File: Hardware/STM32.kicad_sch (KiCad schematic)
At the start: 73 parts, among them IC1 STTS22HTR, U3 STM32L4R5ZITx, Y2 ECS-TXO-2520-33-250-AN-TR, Y3 TG-3541CE_32.7680KXB3

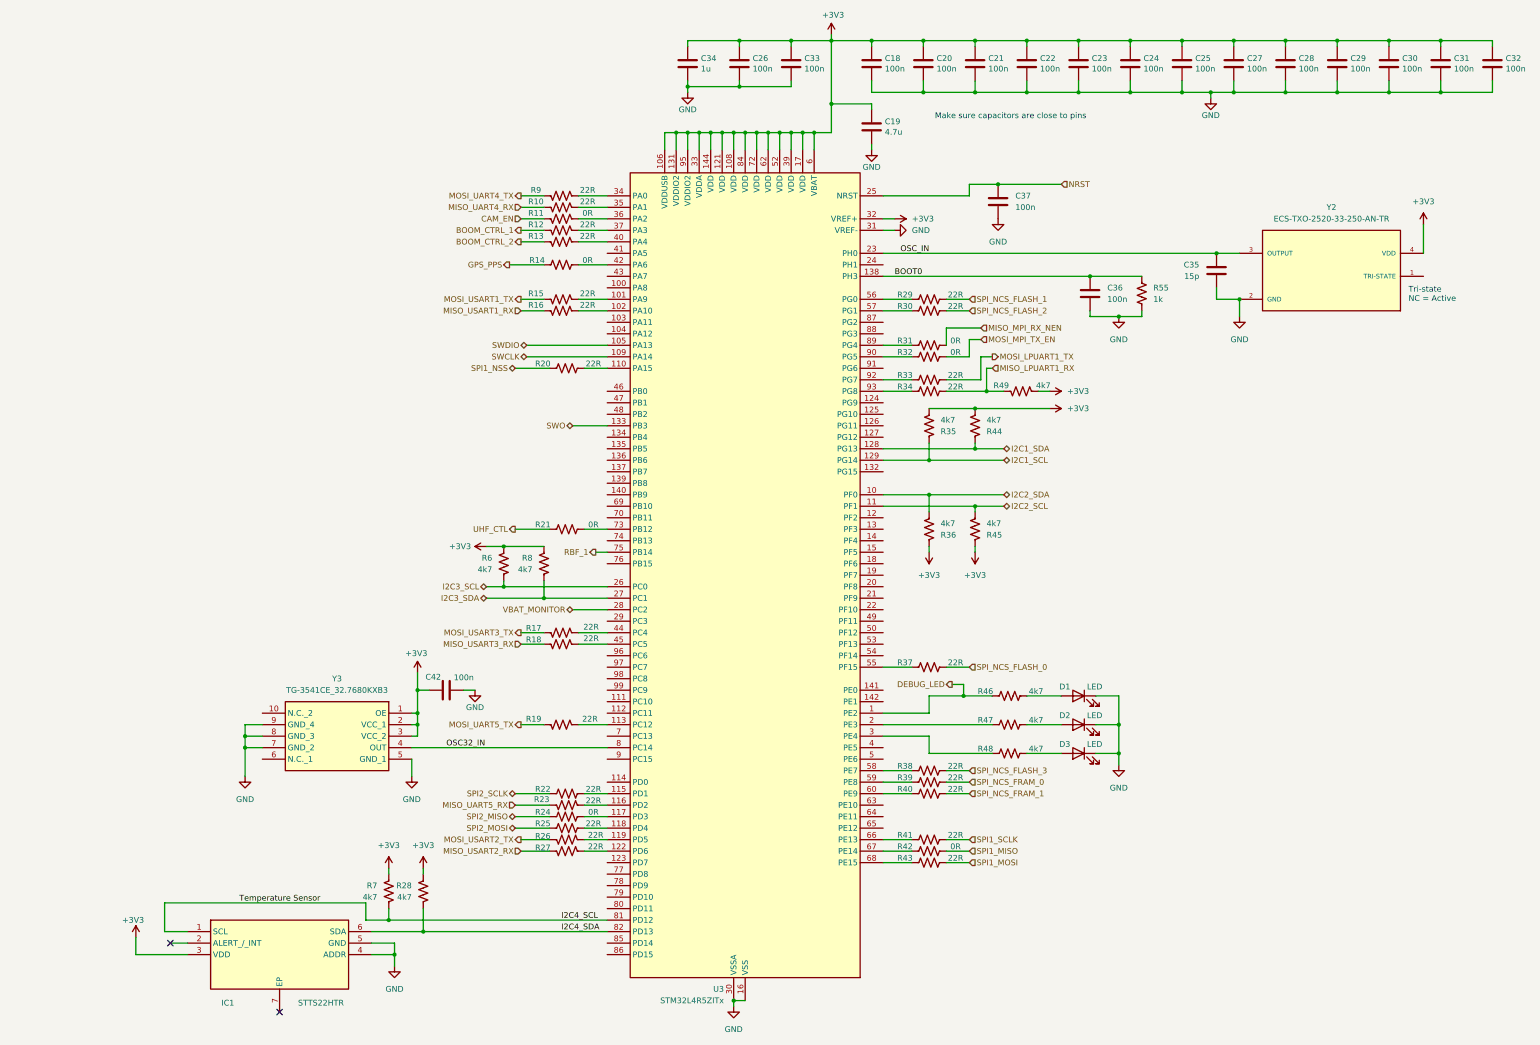
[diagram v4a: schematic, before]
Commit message: Add STM32 Reset Switch & RP2040 I2C pins
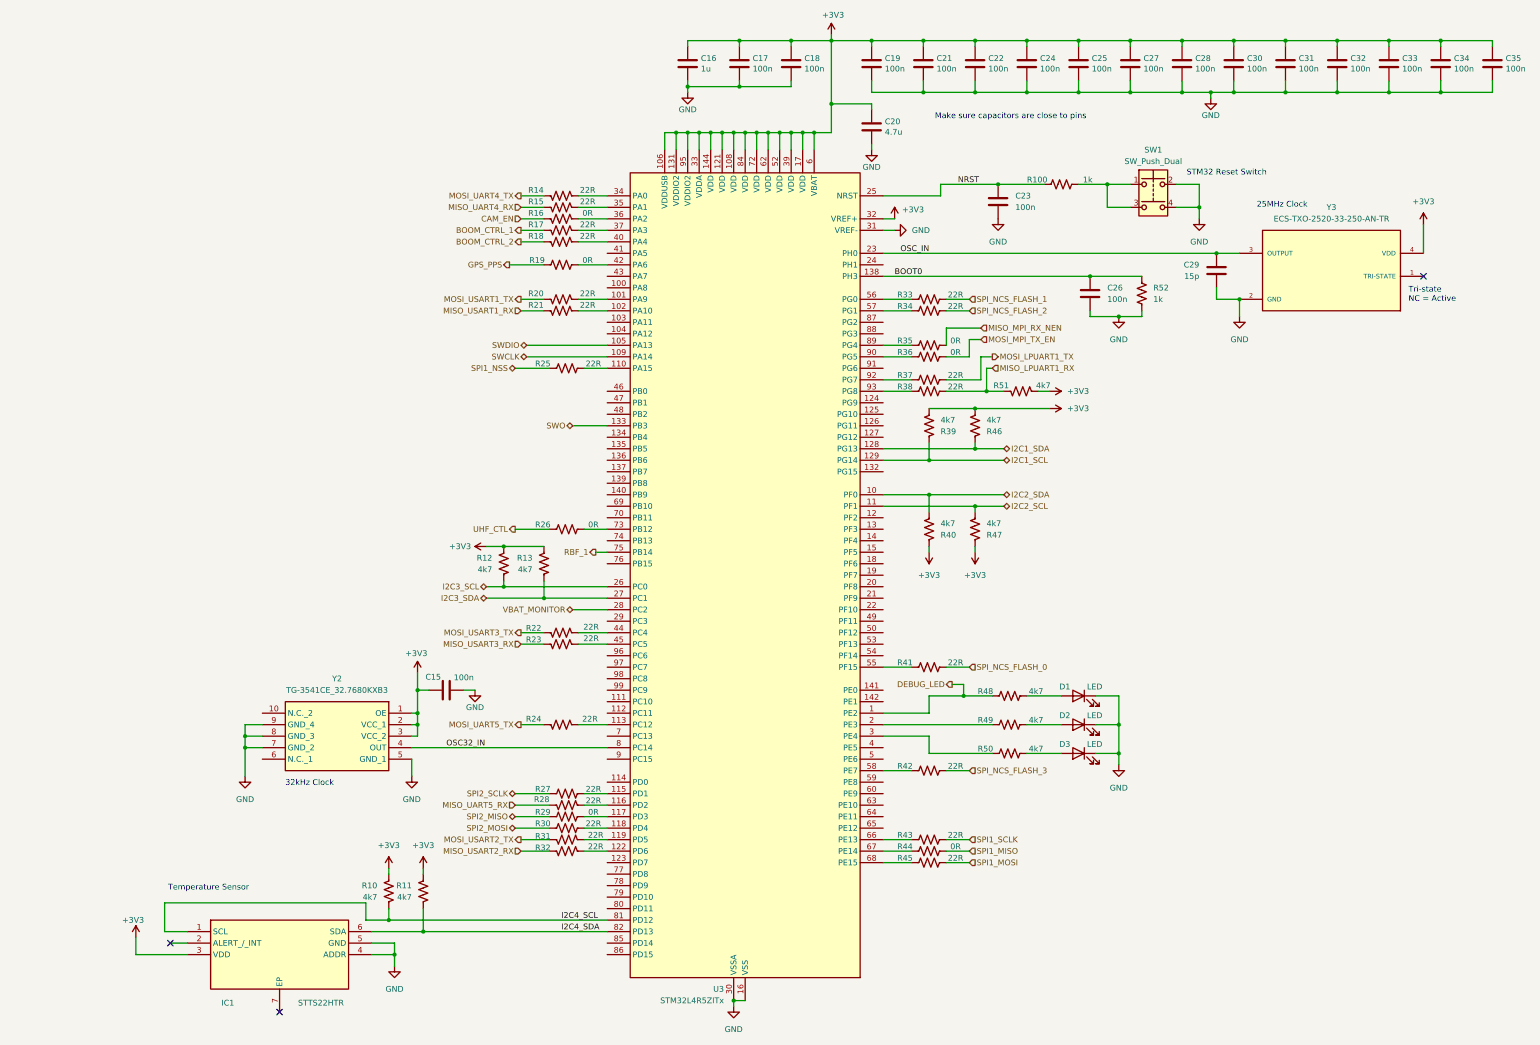
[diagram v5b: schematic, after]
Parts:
- removed R39, R40: 22R, symbol Device:R_US
- added R100: 1k, symbol Device:R_US
- added SW1: SW_Push_Dual, symbol Switch:SW_Push_Dual
- renumbered C42 to C15, C34 to C16, C26 to C17, C33 to C18, C18 to C19, C19 to C20, C20 to C21, C21 to C22, C37 to C23, C22 to C24, C23 to C25, C36 to C26, C24 to C27, C25 to C28, C35 to C29, C27 to C30, C28 to C31, C29 to C32, C30 to C33, C31 to C34, C32 to C35, R7 to R10, R28 to R11, R6 to R12, R8 to R13, R9 to R14, R10 to R15, R11 to R16, R12 to R17, R13 to R18, R14 to R19, R15 to R20, R16 to R21, R17 to R22, R18 to R23, R19 to R24, R20 to R25, R21 to R26, R22 to R27, R23 to R28, R24 to R29, R25 to R30, R26 to R31, R27 to R32, R29 to R33, R30 to R34, R31 to R35, R32 to R36, R33 to R37, R34 to R38, R35 to R39, R36 to R40, R37 to R41, R38 to R42, R41 to R43, R42 to R44, R43 to R45, R44 to R46, R45 to R47, R46 to R48, R47 to R49, R48 to R50, R49 to R51, R55 to R52, Y3 to Y2, Y2 to Y3
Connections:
- net GND: now also SW1.2, SW1.4
- net NRST: now also R100.1
- new net: R100.2, SW1.1, SW1.3
- no-connect marks 2 -> 3
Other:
- note added: "25MHz Clock"
- note added: "32kHz Clock"
- note added: "STM32 Reset Switch"
- note added: "Temperature Sensor"

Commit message: Move ANT to RP2040
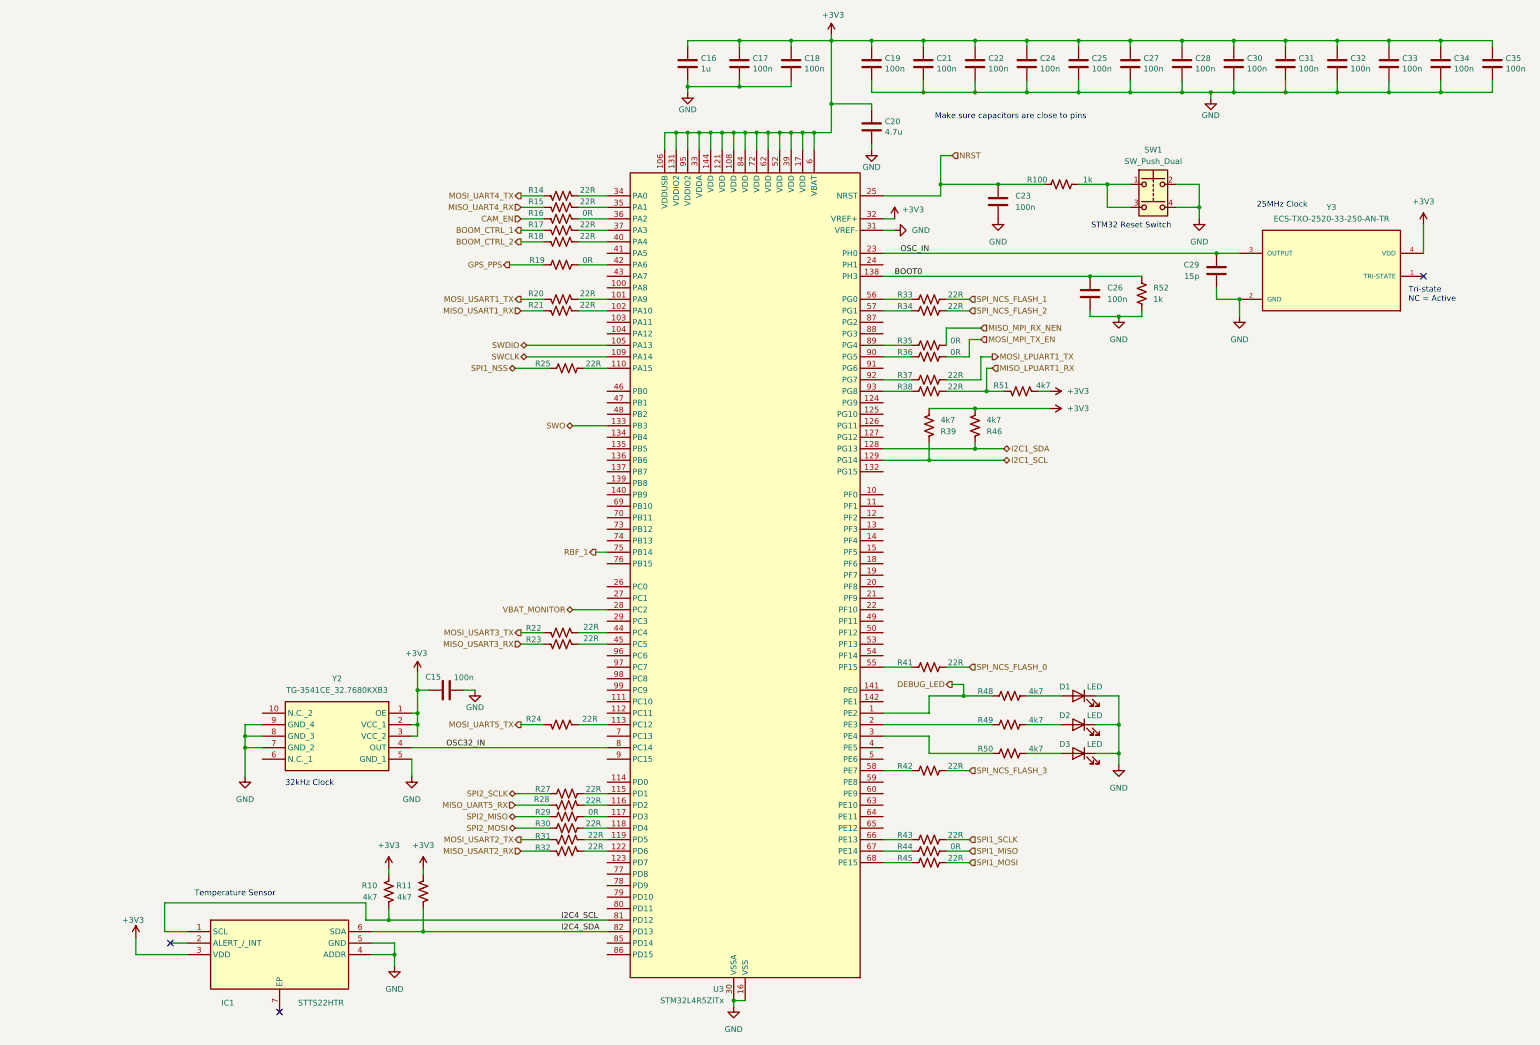
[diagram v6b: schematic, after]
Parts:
- removed R12, R13, R40, R47: 4k7, symbol Device:R_US
- removed R26: 0R, symbol Device:R_US
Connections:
- net I2C2_SCL: no longer names the net of U3.11 (PF1)
- net I2C2_SDA: no longer names the net of U3.10 (PF0)
- net I2C3_SCL: no longer names the net of U3.26 (PC0)
- net I2C3_SDA: no longer names the net of U3.27 (PC1)

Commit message: Add RP2040 SWD
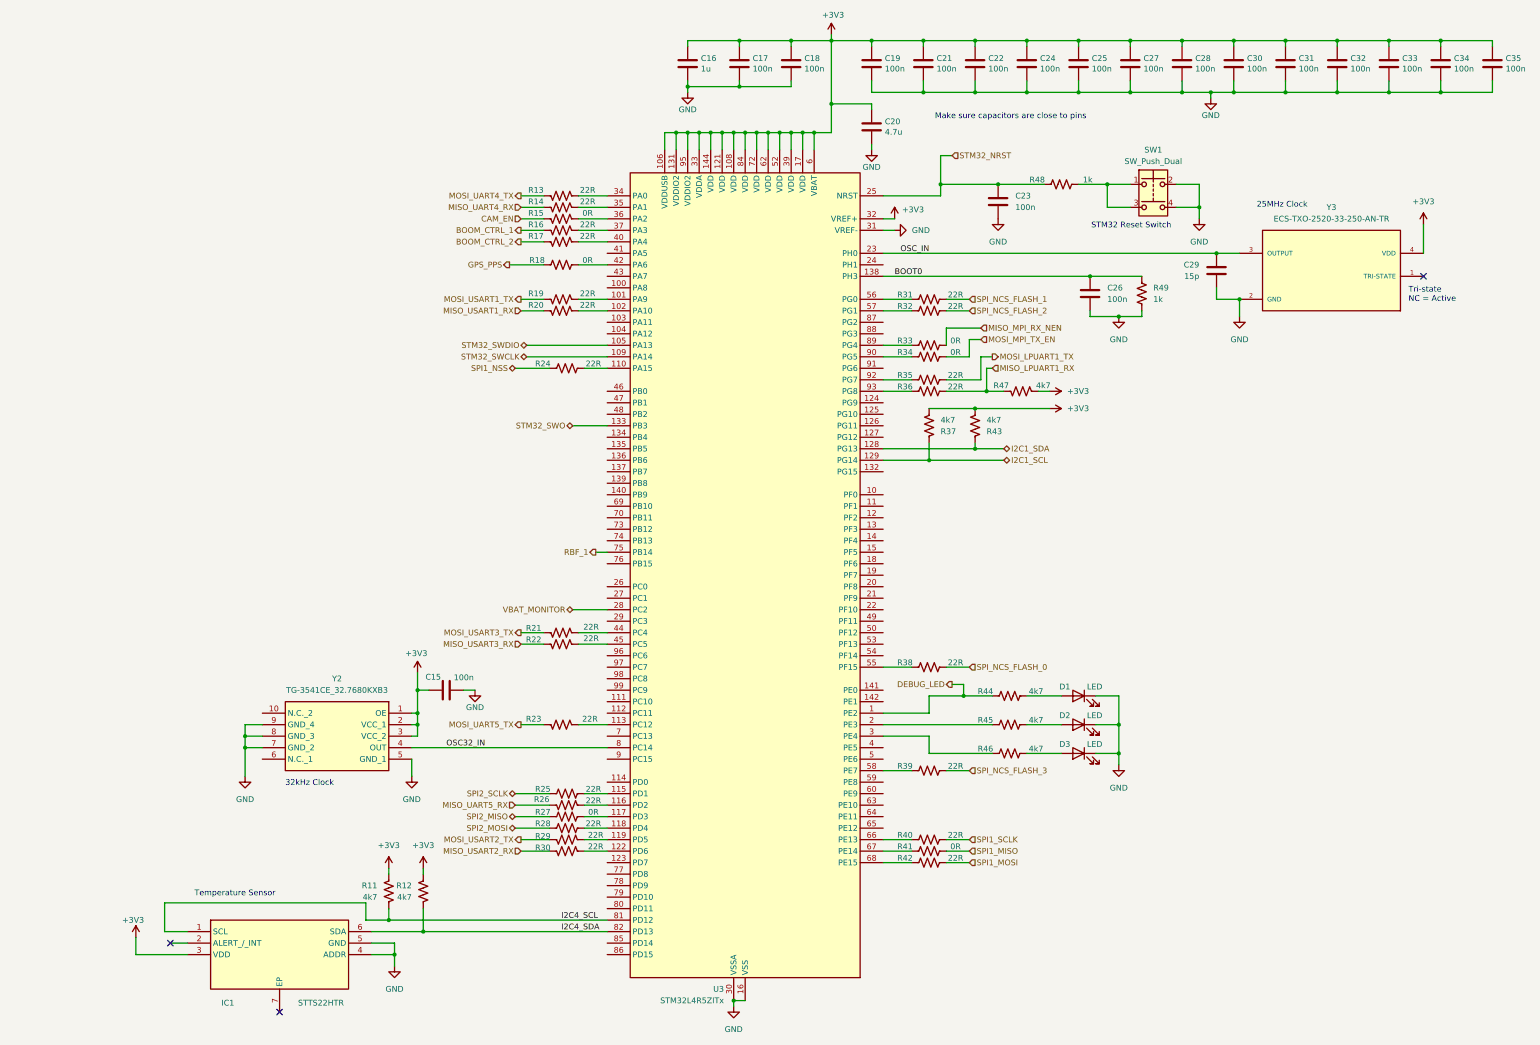
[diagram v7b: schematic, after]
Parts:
- renumbered R10 to R11, R11 to R12, R14 to R13, R15 to R14, R16 to R15, R17 to R16, R18 to R17, R19 to R18, R20 to R19, R21 to R20, R22 to R21, R23 to R22, R24 to R23, R25 to R24, R27 to R25, R28 to R26, R29 to R27, R30 to R28, R31 to R29, R32 to R30, R33 to R31, R34 to R32, R35 to R33, R36 to R34, R37 to R35, R38 to R36, R39 to R37, R41 to R38, R42 to R39, R43 to R40, R44 to R41, R45 to R42, R46 to R43, R48 to R44, R49 to R45, R50 to R46, R51 to R47, R100 to R48, R52 to R49
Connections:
- net NRST renamed STM32_NRST
- net SWCLK renamed STM32_SWCLK
- net SWDIO renamed STM32_SWDIO
- net SWO renamed STM32_SWO

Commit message: Finish schematic v1
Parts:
- removed R37: 4k7, symbol Device:R_US
- added R42: 4k7, symbol Device:R_US
- renumbered R38 to R37, R39 to R38, R40 to R39, R41 to R40, R42 to R41
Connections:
- net +3V3: now also R42.2
- net I2C1_SDA: no longer R43.1
- net I2C4_SCL: no longer IC1.1 (SCL), R11.2
- net I2C4_SDA: no longer IC1.6 (SDA), R12.2
- net I2C2_SDA: now reaches U3.10 (PF0)
- net I2C2_SDA: now also R43.1
- net I2C2_SCL: now reaches U3.11 (PF1)
- net I2C2_SCL: now also R42.1
- net I2C3_SCL: now reaches U3.26 (PC0)
- net I2C3_SCL: now also IC1.1 (SCL), R11.2
- net I2C3_SDA: now reaches U3.27 (PC1)
- net I2C3_SDA: now also IC1.6 (SDA), R12.2
- no-connect marks 3 -> 7
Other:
- moved on the sheet: IC1, R11, R12
